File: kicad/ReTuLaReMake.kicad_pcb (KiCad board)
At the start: 2 copper layers, 54 x 26 mm, 23 parts, among them J1 40 Pin DIP Header, U1 ATF1508AS-10AU100

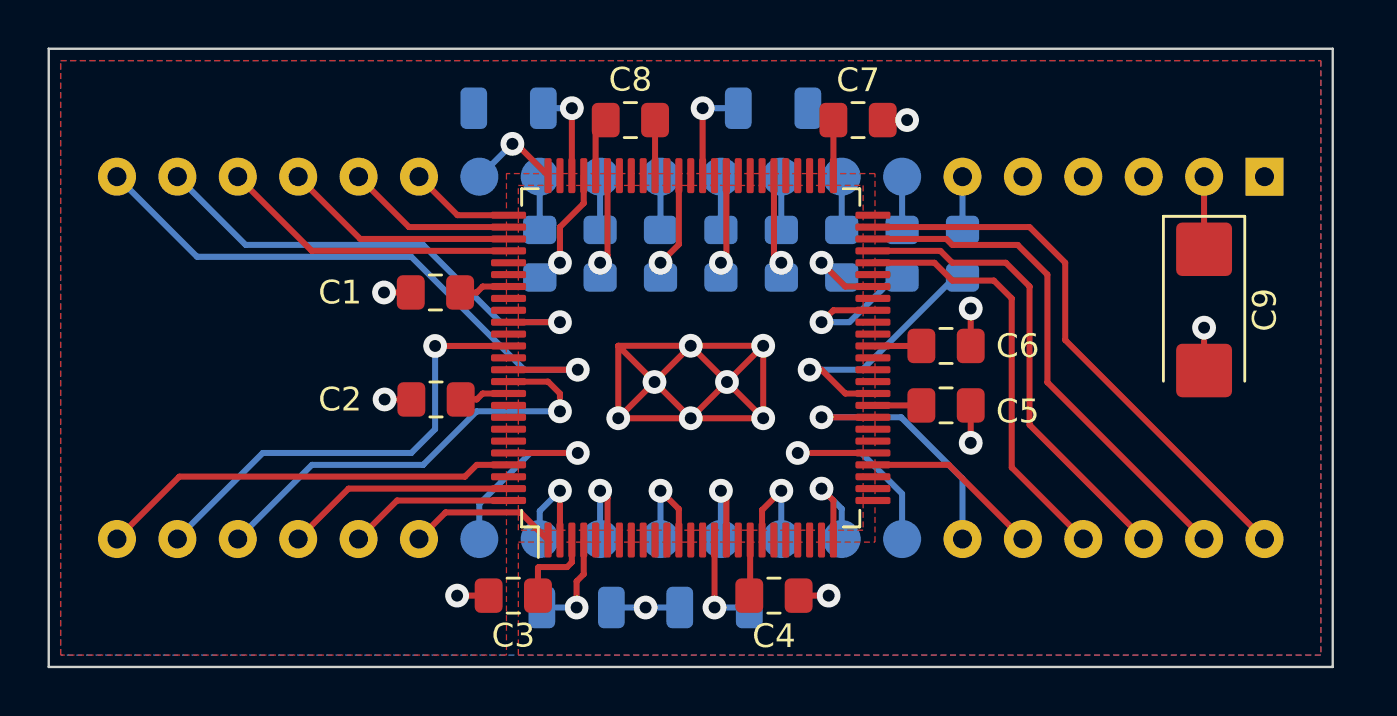
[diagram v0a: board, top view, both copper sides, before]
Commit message: KiCAD: Added JTAG Connector
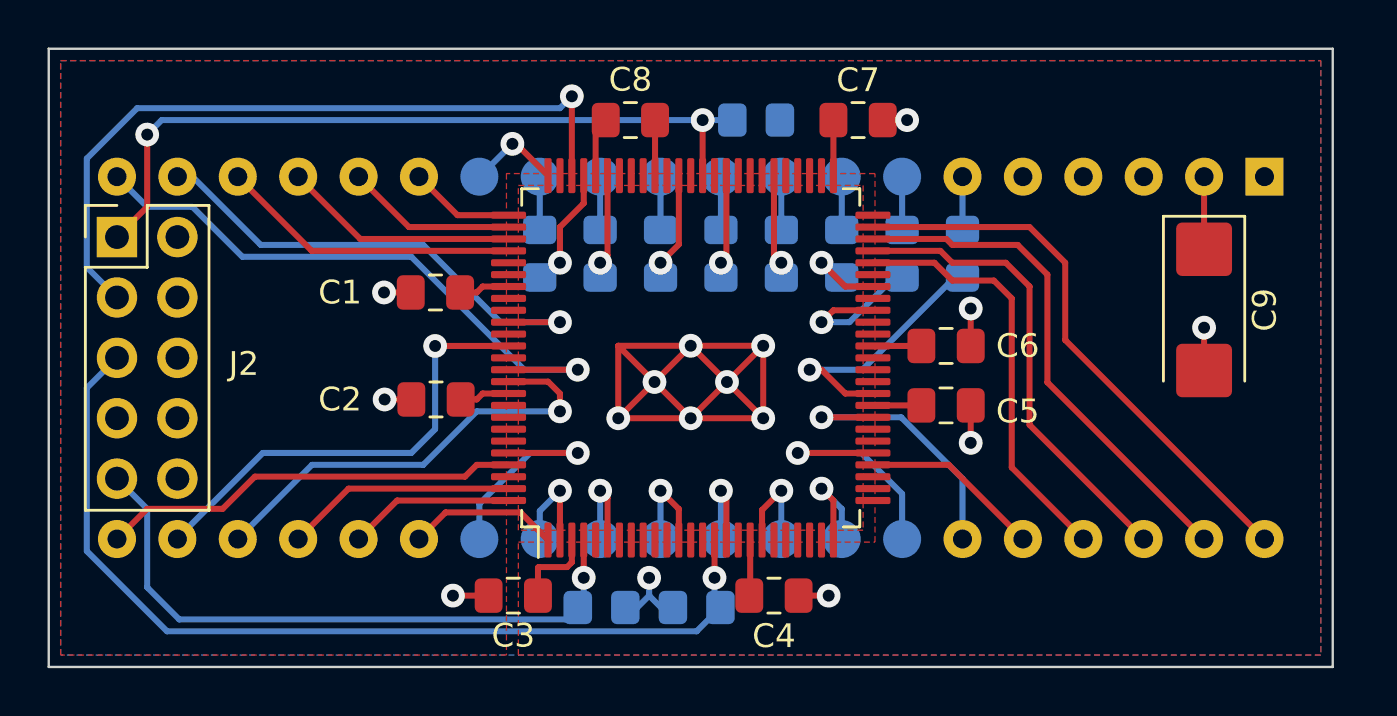
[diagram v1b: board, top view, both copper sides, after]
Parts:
- removed R10: NF, Resistor_SMD:R_1206_3216Metric
- added J2: Conn_02x05_Odd_Even, Connector_PinHeader_2.54mm:PinHeader_2x05_P2.54mm_Vertical, F.Cu at (102.9, 114.3)
- R11, R12, R9: footprint Resistor_SMD:R_1206_3216Metric -> Resistor_SMD:R_0805_2012Metric_Pad1.20x1.40mm_HandSolder
- moved R12 1.05 mm to (123.2, 129.9)
- moved R9 0.87 mm to (129.8, 109.4)
- moved R11 0.75 mm to (127.2, 129.9)
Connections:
- net Net-(R11-Pad1) renamed /TMS
- net Net-(R12-Pad2) renamed /TDI
- net Net-(R9-Pad1) renamed /TCK
- U1 pad 73: Net-(R10-Pad1) -> /TDO
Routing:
- net /TMS: track 4.30 -> 40.1 mm
- net /TDO: track 0.00 -> 31.2 mm, vias 0 -> 1
- net /TCK: track 4.34 -> 32.0 mm, vias 1 -> 2
- net /TDI: track 4.42 -> 26.9 mm
- net Net-(R10-Pad1): track 4.04 -> 0.00 mm, vias 1 -> 0
- net /HO2: track 20.8 -> 20.2 mm

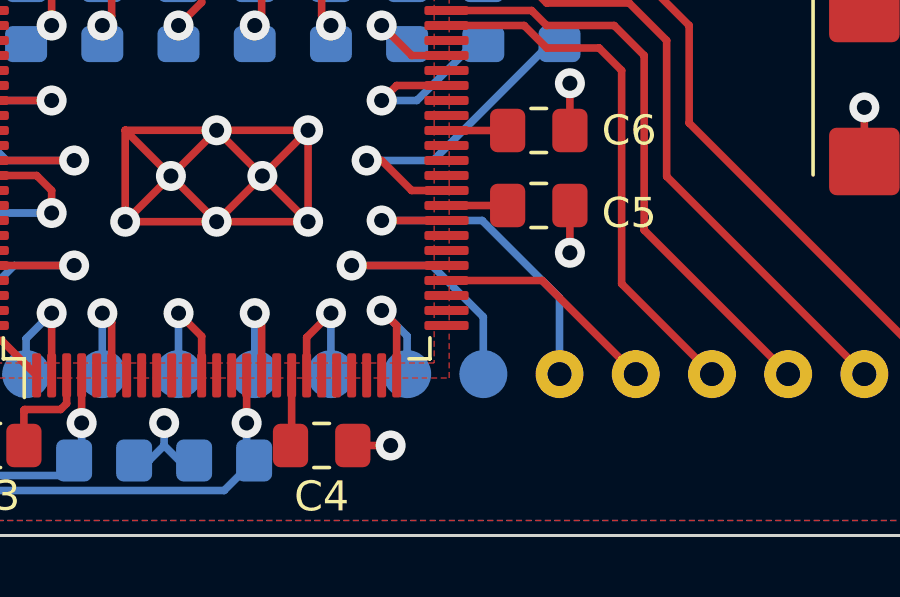
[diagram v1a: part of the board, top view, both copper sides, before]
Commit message: KiCAD: Update pins for p_data2/1/0
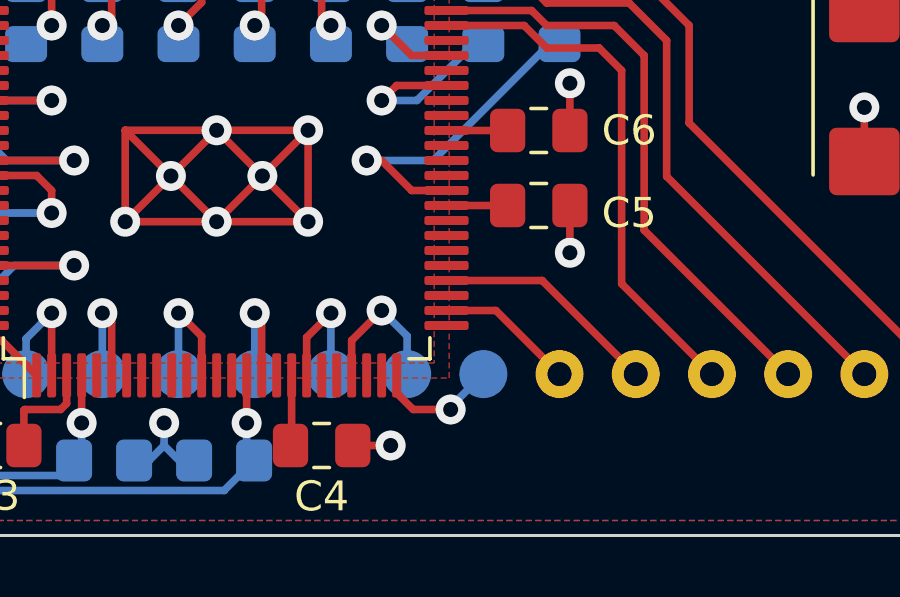
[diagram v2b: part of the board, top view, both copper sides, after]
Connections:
- U1 pad 22: GND -> /PD2
- U1 pad 25: /PD2 -> /PD1
- U1 pad 27: GND -> /PD0
- U1 pad 30: /PD1 -> GND
- U1 pad 33: /PD0 -> GND
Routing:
- net /PD0: track 11.7 -> 4.65 mm, vias 1 -> 0
- net /PD1: track 10.2 -> 4.25 mm
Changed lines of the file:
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@@
       (net 2 "GND") (pinfunction "I/O_15") (pintype "passive"))
     (pad "22" smd roundrect (at -7.6625 4.5 90) (size 1.475 0.3) (layers "F.Cu" "F.Paste" "F.Mask") (roundrect_rratio 0.25)
-      (net 2 "GND") (pinfunction "I/O_16") (pintype "passive"))
+      (net 32 "/PD2") (pinfunction "I/O_16") (pintype "passive"))
     (pad "23" smd roundrect (at -7.6625 5 90) (size 1.475 0.3) (layers "F.Cu" "F.Paste" "F.Mask") (roundrect_rratio 0.25)
       (net 2 "GND") (pinfunction "I/O_17") (pintype "passive"))
@@
       (net 2 "GND") (pinfunction "I/O_18") (pintype "passive"))
     (pad "25" smd roundrect (at -7.6625 6 90) (size 1.475 0.3) (layers "F.Cu" "F.Paste" "F.Mask") (roundrect_rratio 0.25)
-      (net 32 "/PD2") (pinfunction "I/O_19") (pintype "passive"))
+      (net 33 "/PD1") (pinfunction "I/O_19") (pintype "passive"))
     (pad "26" smd roundrect (at -6 7.6625 90) (size 0.3 1.475) (layers "F.Cu" "F.Paste" "F.Mask") (roundrect_rratio 0.25)
       (net 2 "GND") (pinfunction "GND_2") (pintype "passive"))
     (pad "27" smd roundrect (at -5.5 7.6625 90) (size 0.3 1.475) (layers "F.Cu" "F.Paste" "F.Mask") (roundrect_rratio 0.25)
-      (net 2 "GND") (pinfunction "I/O_20") (pintype "passive"))
+      (net 34 "/PD0") (pinfunction "I/O_20") (pintype "passive"))
     (pad "28" smd roundrect (at -5 7.6625 90) (size 0.3 1.475) (layers "F.Cu" "F.Paste" "F.Mask") (roundrect_rratio 0.25)
       (net 2 "GND") (pinfunction "I/O_21") (pintype "passive"))
@@
       (net 35 "/PIRQ") (pinfunction "I/O_22") (pintype "passive"))
     (pad "30" smd roundrect (at -4 7.6625 90) (size 0.3 1.475) (layers "F.Cu" "F.Paste" "F.Mask") (roundrect_rratio 0.25)
-      (net 33 "/PD1") (pinfunction "I/O_23") (pintype "passive"))
+      (net 2 "GND") (pinfunction "I/O_23") (pintype "passive"))
     (pad "31" smd roundrect (at -3.5 7.6625 90) (size 0.3 1.475) (layers "F.Cu" "F.Paste" "F.Mask") (roundrect_rratio 0.25)
       (net 2 "GND") (pinfunction "I/O_24") (pintype "passive"))
@@
       (net 2 "GND") (pinfunction "I/O_25") (pintype "passive"))
     (pad "33" smd roundrect (at -2.5 7.6625 90) (size 0.3 1.475) (layers "F.Cu" "F.Paste" "F.Mask") (roundrect_rratio 0.25)
-      (net 34 "/PD0") (pinfunction "I/O_26") (pintype "passive"))
+      (net 2 "GND") (pinfunction "I/O_26") (pintype "passive"))
     (pad "34" smd roundrect (at -2 7.6625 90) (size 0.3 1.475) (layers "F.Cu" "F.Paste" "F.Mask") (roundrect_rratio 0.25)
       (net 1 "VCC") (pinfunction "VCCIO_3") (pintype "passive"))
@@
   (via (at 130.81 124.968) (size 1) (drill 0.5) (layers "F.Cu" "B.Cu") (net 31))
   (segment (start 130.81 127) (end 130.81 124.968) (width 0.254) (layer "B.Cu") (net 31))
-  (segment (start 133 125.38) (end 133 127.0425) (width 0.254) (layer "F.Cu") (net 32))
-  (segment (start 132.5 124.88) (end 133 125.38) (width 0.254) (layer "F.Cu") (net 32))
+  (segment (start 131.5 125.88) (end 131.5 127.0425) (width 0.254) (layer "F.Cu") (net 32))
+  (segment (start 132.5 124.88) (end 131.5 125.88) (width 0.254) (layer "F.Cu") (net 32))
   (via (at 132.5 124.88) (size 1) (drill 0.5) (layers "F.Cu" "B.Cu") (net 32))
   (segment (start 132.5 124.88) (end 133.35 125.73) (width 0.254) (layer "B.Cu") (net 32))
   (segment (start 133.35 125.73) (end 133.35 127) (width 0.254) (layer "B.Cu") (net 32))
-  (segment (start 131.5 123.38) (end 134.6625 123.38) (width 0.254) (layer "F.Cu") (net 33))
-  (via (at 131.5 123.38) (size 1) (drill 0.5) (layers "F.Cu" "B.Cu") (net 33))
-  (segment (start 131.5 123.38) (end 134.175 123.38) (width 0.254) (layer "B.Cu") (net 33))
-  (segment (start 134.175 123.38) (end 135.89 125.095) (width 0.254) (layer "B.Cu") (net 33))
-  (segment (start 135.89 125.095) (end 135.89 127) (width 0.254) (layer "B.Cu") (net 33))
-  (segment (start 132.5 121.88) (end 134.6625 121.88) (width 0.254) (layer "F.Cu") (net 34))
-  (via (at 132.5 121.88) (size 1) (drill 0.5) (layers "F.Cu" "B.Cu") (net 34))
-  (segment (start 135.85 121.88) (end 138.43 124.46) (width 0.254) (layer "B.Cu") (net 34))
-  (segment (start 132.5 121.88) (end 135.85 121.88) (width 0.254) (layer "B.Cu") (net 34))
-  (segment (start 138.43 124.46) (end 138.43 127) (width 0.254) (layer "B.Cu") (net 34))
+  (segment (start 134.8 128.18) (end 133.55 128.18) (width 0.254) (layer "F.Cu") (net 33))
+  (segment (start 133.55 128.18) (end 133 127.63) (width 0.254) (layer "F.Cu") (net 33))
+  (segment (start 133 127.63) (end 133 127.0425) (width 0.254) (layer "F.Cu") (net 33))
+  (via (at 134.8 128.18) (size 1) (drill 0.5) (layers "F.Cu" "B.Cu") (net 33))
+  (segment (start 134.8 128.18) (end 134.8 128.09) (width 0.254) (layer "B.Cu") (net 33))
+  (segment (start 134.8 128.09) (end 135.89 127) (width 0.254) (layer "B.Cu") (net 33))
+  (segment (start 134.6625 124.88) (end 136.31 124.88) (width 0.254) (layer "F.Cu") (net 34))
+  (segment (start 136.31 124.88) (end 138.43 127) (width 0.254) (layer "F.Cu") (net 34))
   (segment (start 137.85 123.88) (end 140.97 127) (width 0.254) (layer "F.Cu") (net 35))
   (segment (start 134.6625 123.88) (end 137.85 123.88) (width 0.254) (layer "F.Cu") (net 35))

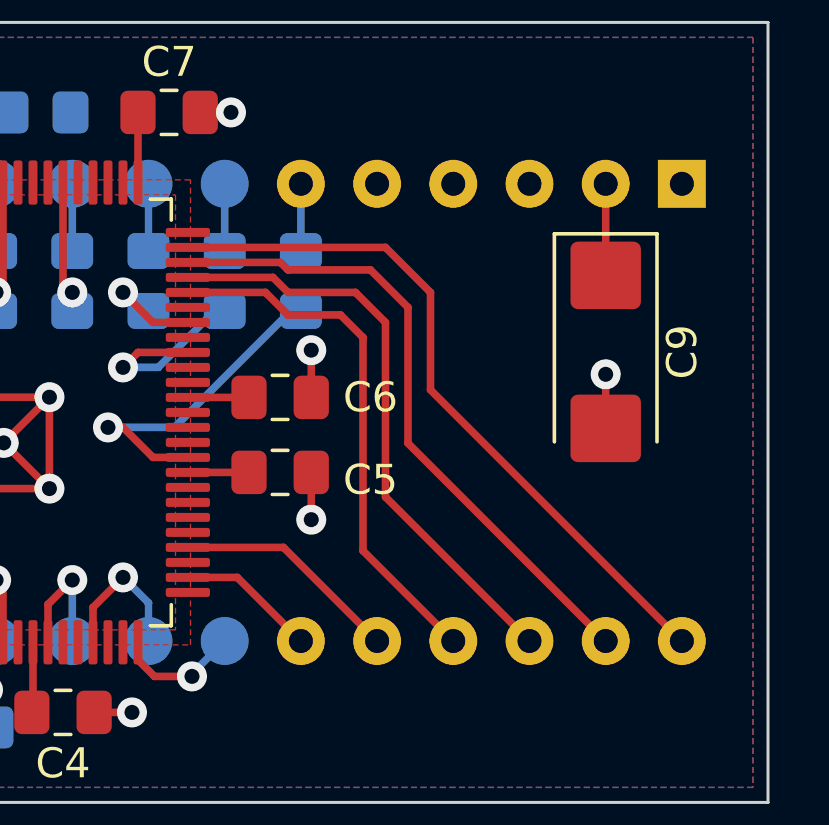
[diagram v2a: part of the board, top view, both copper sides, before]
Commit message: KiCAD: Add schottky diodes
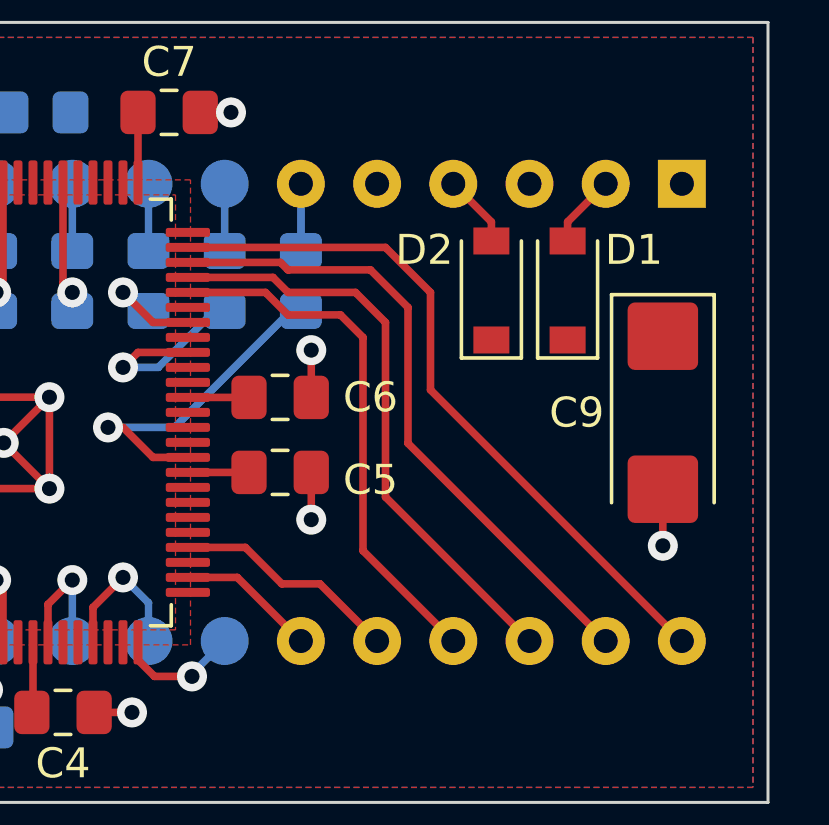
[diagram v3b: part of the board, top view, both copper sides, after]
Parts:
- added D1: MBR130, Diode_SMD:D_SOD-123, F.Cu at (147.3, 115.3)
- added D2: MBR130, Diode_SMD:D_SOD-123, F.Cu at (144.8, 115.3)
- moved C9 2.78 mm to (150.5, 119.4)
- renumbered R12 to R10
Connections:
- J1 pad 2: VCC -> Net-(D1-Pad2)
- J1 pad 4: unconnected-(J1-Pad4) -> Net-(D2-Pad2)
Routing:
- net VCC: track 24.6 -> 22.1 mm
- net Net-(D2-Pad2): track 0.00 -> 2.43 mm
- net Net-(D1-Pad2): track 0.00 -> 2.43 mm

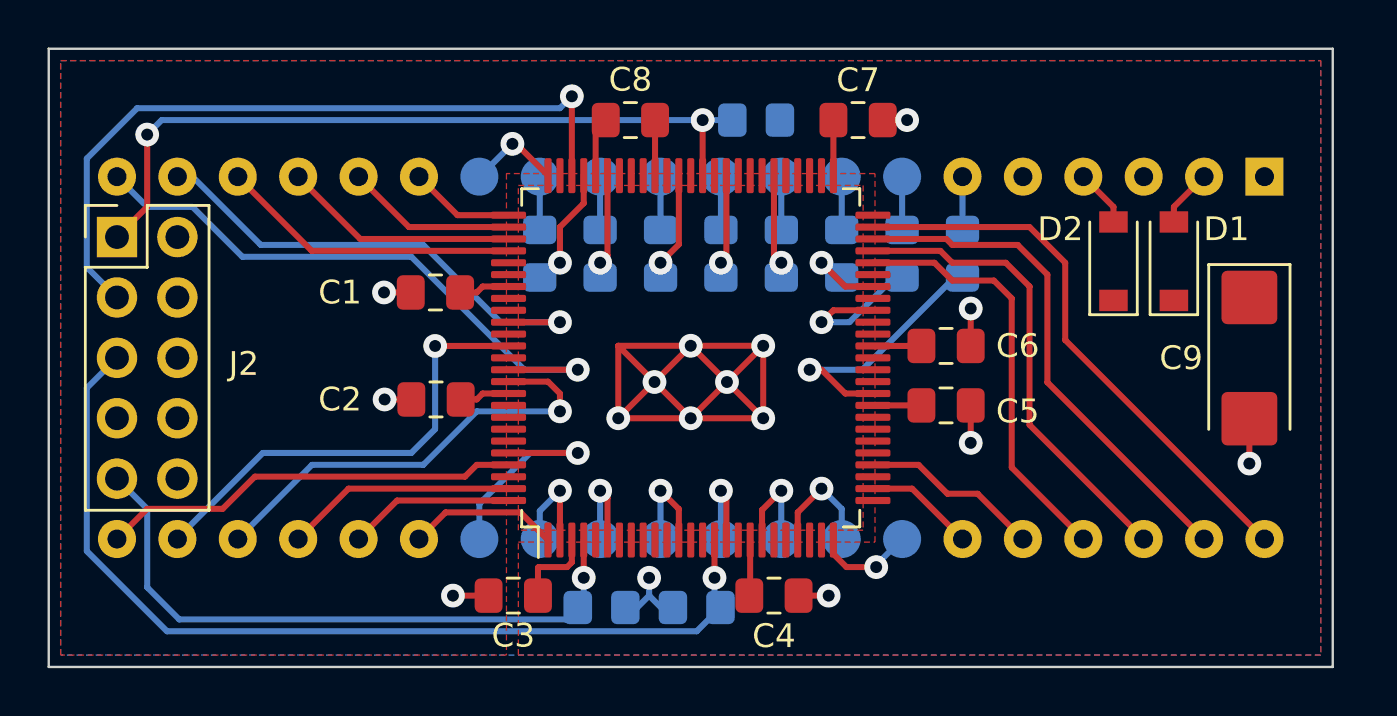
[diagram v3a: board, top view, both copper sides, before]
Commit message: KiCAD: Add 12V OE1 Test Point
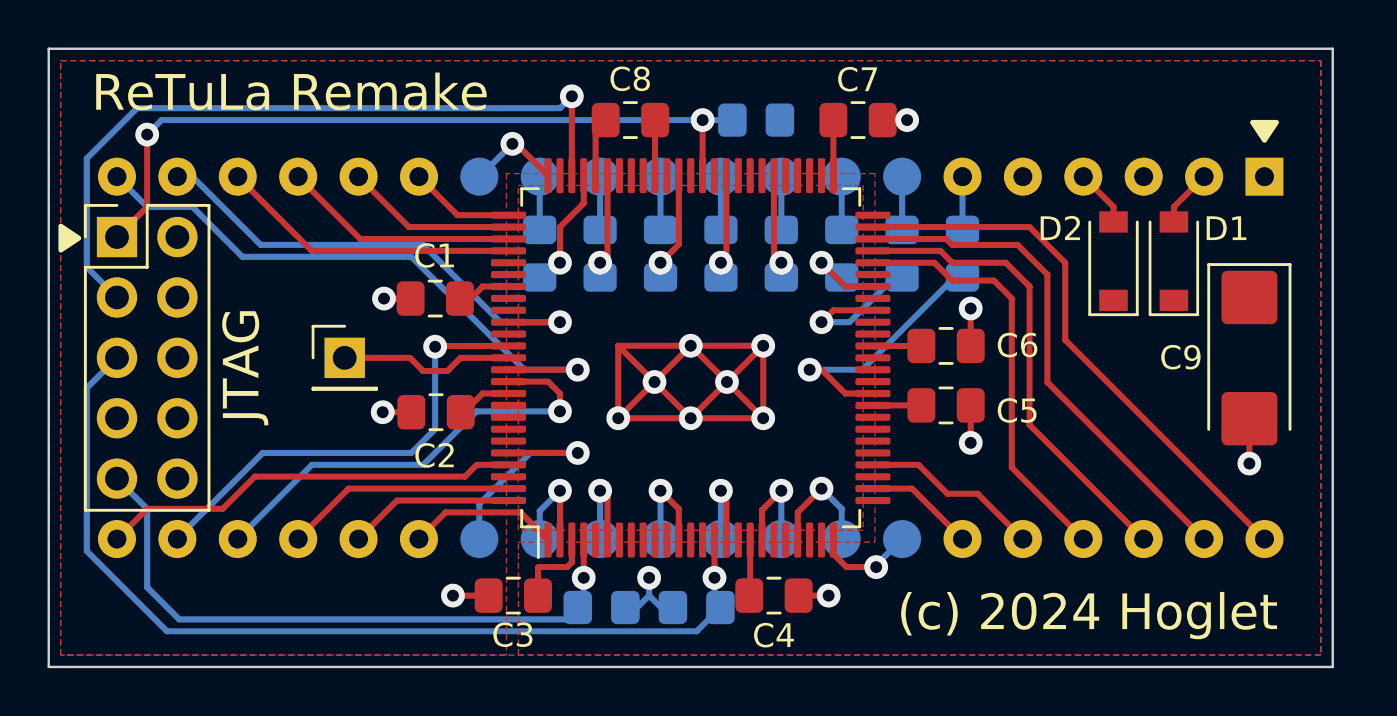
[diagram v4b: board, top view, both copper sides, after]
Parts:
- added J3: Conn_01x01_Male, Connector_PinHeader_2.54mm:PinHeader_1x01_P2.54mm_Vertical, F.Cu at (112.4, 119.4)
- moved C2 0.54 mm to (116.3, 121.7)
- moved C1 0.26 mm to (116.3, 116.9)
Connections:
- U1 pad 88: GND -> Net-(J3-Pad1)
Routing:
- net Net-(J3-Pad1): track 0.00 -> 7.35 mm
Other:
- board text added: "(c) 2024 Hoglet"
- board text added: "JTAG"
- board text added: "ReTuLa Remake"
